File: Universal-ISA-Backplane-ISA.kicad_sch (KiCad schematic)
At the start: 1 part, among them J301 Bus_ISA_16bit

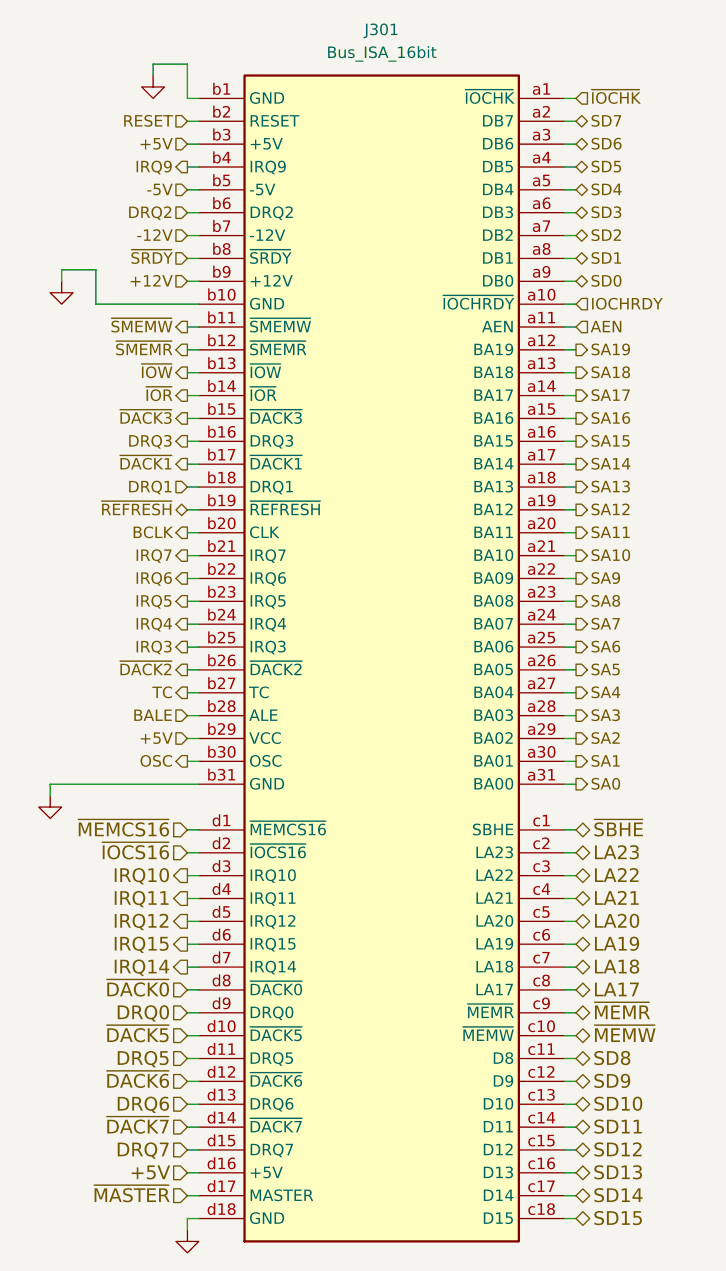
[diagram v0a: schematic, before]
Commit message: PC/104 and ISA connector fixes
And further development
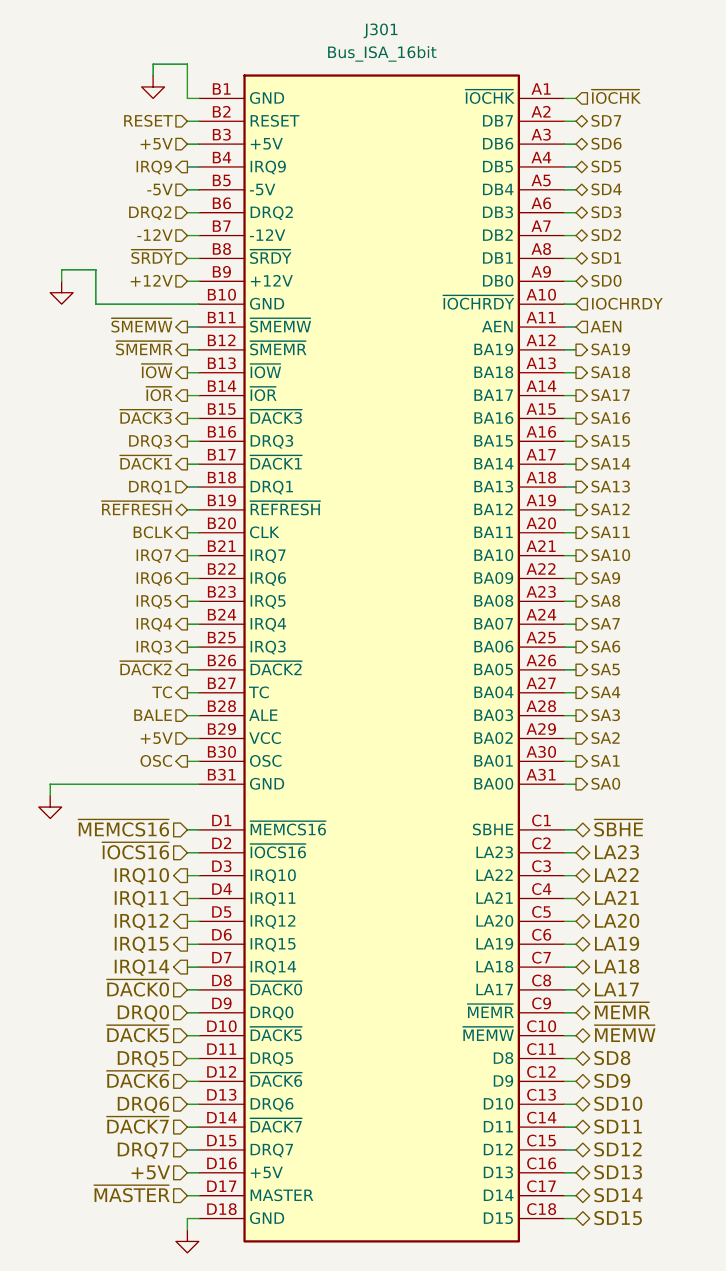
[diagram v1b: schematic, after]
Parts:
- J301: symbol Connector1:Bus_ISA_16bit -> Universal-ISA-Backplane-symbols:Bus_ISA_16bit
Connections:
- net +12V: now also J301.B9 (+12V); no longer J301.b9 (+12V)
- net +5V: now also J301.B29 (VCC), J301.B3 (+5V), J301.D16 (+5V); no longer J301.b29 (VCC), J301.b3 (+5V), J301.d16 (+5V)
- net -12V: now also J301.B7 (-12V); no longer J301.b7 (-12V)
- net -5V: now also J301.B5 (-5V); no longer J301.b5 (-5V)
- net AEN: now also J301.A11 (AEN); no longer J301.a11 (AEN)
- net BALE: now also J301.B28 (ALE); no longer J301.b28 (ALE)
- net BCLK: now also J301.B20 (CLK); no longer J301.b20 (CLK)
- net DRQ0: now also J301.D9 (DRQ0); no longer J301.d9 (DRQ0)
- net DRQ1: now also J301.B18 (DRQ1); no longer J301.b18 (DRQ1)
- net DRQ2: now also J301.B6 (DRQ2); no longer J301.b6 (DRQ2)
- net DRQ3: now also J301.B16 (DRQ3); no longer J301.b16 (DRQ3)
- net DRQ5: now also J301.D11 (DRQ5); no longer J301.d11 (DRQ5)
- net DRQ6: now also J301.D13 (DRQ6); no longer J301.d13 (DRQ6)
- net DRQ7: now also J301.D15 (DRQ7); no longer J301.d15 (DRQ7)
- net GND: now also J301.B1 (GND), J301.B10 (GND), J301.B31 (GND), J301.D18 (GND); no longer J301.b1 (GND), J301.b10 (GND), J301.b31 (GND), J301.d18 (GND)
- net IOCHRDY: now also J301.A10 (~{IOCHRDY}); no longer J301.a10 (~{IOCHRDY})
- net IRQ10: now also J301.D3 (IRQ10); no longer J301.d3 (IRQ10)
- net IRQ11: now also J301.D4 (IRQ11); no longer J301.d4 (IRQ11)
- net IRQ12: now also J301.D5 (IRQ12); no longer J301.d5 (IRQ12)
- net IRQ14: now also J301.D7 (IRQ14); no longer J301.d7 (IRQ14)
- net IRQ15: now also J301.D6 (IRQ15); no longer J301.d6 (IRQ15)
- net IRQ3: now also J301.B25 (IRQ3); no longer J301.b25 (IRQ3)
- net IRQ4: now also J301.B24 (IRQ4); no longer J301.b24 (IRQ4)
- net IRQ5: now also J301.B23 (IRQ5); no longer J301.b23 (IRQ5)
- net IRQ6: now also J301.B22 (IRQ6); no longer J301.b22 (IRQ6)
- net IRQ7: now also J301.B21 (IRQ7); no longer J301.b21 (IRQ7)
- net IRQ9: now also J301.B4 (IRQ9); no longer J301.b4 (IRQ9)
- net LA17: now also J301.C8 (LA17); no longer J301.c8 (LA17)
- net LA18: now also J301.C7 (LA18); no longer J301.c7 (LA18)
- net LA19: now also J301.C6 (LA19); no longer J301.c6 (LA19)
- net LA20: now also J301.C5 (LA20); no longer J301.c5 (LA20)
- net LA21: now also J301.C4 (LA21); no longer J301.c4 (LA21)
- net LA22: now also J301.C3 (LA22); no longer J301.c3 (LA22)
- net LA23: now also J301.C2 (LA23); no longer J301.c2 (LA23)
- net OSC: now also J301.B30 (OSC); no longer J301.b30 (OSC)
- net RESET: now also J301.B2 (RESET); no longer J301.b2 (RESET)
- net SA0: now also J301.A31 (BA00); no longer J301.a31 (BA00)
- net SA1: now also J301.A30 (BA01); no longer J301.a30 (BA01)
- net SA10: now also J301.A21 (BA10); no longer J301.a21 (BA10)
- net SA11: now also J301.A20 (BA11); no longer J301.a20 (BA11)
- net SA12: now also J301.A19 (BA12); no longer J301.a19 (BA12)
- net SA13: now also J301.A18 (BA13); no longer J301.a18 (BA13)
- net SA14: now also J301.A17 (BA14); no longer J301.a17 (BA14)
- net SA15: now also J301.A16 (BA15); no longer J301.a16 (BA15)
- net SA16: now also J301.A15 (BA16); no longer J301.a15 (BA16)
- net SA17: now also J301.A14 (BA17); no longer J301.a14 (BA17)
- net SA18: now also J301.A13 (BA18); no longer J301.a13 (BA18)
- net SA19: now also J301.A12 (BA19); no longer J301.a12 (BA19)
- net SA2: now also J301.A29 (BA02); no longer J301.a29 (BA02)
- net SA3: now also J301.A28 (BA03); no longer J301.a28 (BA03)
- net SA4: now also J301.A27 (BA04); no longer J301.a27 (BA04)
- net SA5: now also J301.A26 (BA05); no longer J301.a26 (BA05)
- net SA6: now also J301.A25 (BA06); no longer J301.a25 (BA06)
- net SA7: now also J301.A24 (BA07); no longer J301.a24 (BA07)
- net SA8: now also J301.A23 (BA08); no longer J301.a23 (BA08)
- net SA9: now also J301.A22 (BA09); no longer J301.a22 (BA09)
- net SD0: now also J301.A9 (DB0); no longer J301.a9 (DB0)
- net SD1: now also J301.A8 (DB1); no longer J301.a8 (DB1)
- net SD10: now also J301.C13 (D10); no longer J301.c13 (D10)
- net SD11: now also J301.C14 (D11); no longer J301.c14 (D11)
- net SD12: now also J301.C15 (D12); no longer J301.c15 (D12)
- net SD13: now also J301.C16 (D13); no longer J301.c16 (D13)
- net SD14: now also J301.C17 (D14); no longer J301.c17 (D14)
- net SD15: now also J301.C18 (D15); no longer J301.c18 (D15)
- net SD2: now also J301.A7 (DB2); no longer J301.a7 (DB2)
- net SD3: now also J301.A6 (DB3); no longer J301.a6 (DB3)
- net SD4: now also J301.A5 (DB4); no longer J301.a5 (DB4)
- net SD5: now also J301.A4 (DB5); no longer J301.a4 (DB5)
- net SD6: now also J301.A3 (DB6); no longer J301.a3 (DB6)
- net SD7: now also J301.A2 (DB7); no longer J301.a2 (DB7)
- net SD8: now also J301.C11 (D8); no longer J301.c11 (D8)
- net SD9: now also J301.C12 (D9); no longer J301.c12 (D9)
- net TC: now also J301.B27 (TC); no longer J301.b27 (TC)
- net ~{DACK0}: now also J301.D8 (~{DACK0}); no longer J301.d8 (~{DACK0})
- net ~{DACK1}: now also J301.B17 (~{DACK1}); no longer J301.b17 (~{DACK1})
- net ~{DACK2}: now also J301.B26 (~{DACK2}); no longer J301.b26 (~{DACK2})
- net ~{DACK3}: now also J301.B15 (~{DACK3}); no longer J301.b15 (~{DACK3})
- net ~{DACK5}: now also J301.D10 (~{DACK5}); no longer J301.d10 (~{DACK5})
- net ~{DACK6}: now also J301.D12 (~{DACK6}); no longer J301.d12 (~{DACK6})
- net ~{DACK7}: now also J301.D14 (~{DACK7}); no longer J301.d14 (~{DACK7})
- net ~{IOCHK}: now also J301.A1 (~{IOCHK}); no longer J301.a1 (~{IOCHK})
- net ~{IOCS16}: now also J301.D2 (~{IOCS16}); no longer J301.d2 (~{IOCS16})
- net ~{IOR}: now also J301.B14 (~{IOR}); no longer J301.b14 (~{IOR})
- net ~{IOW}: now also J301.B13 (~{IOW}); no longer J301.b13 (~{IOW})
- net ~{MASTER}: now also J301.D17 (MASTER); no longer J301.d17 (MASTER)
- net ~{MEMCS16}: now also J301.D1 (~{MEMCS16}); no longer J301.d1 (~{MEMCS16})
- net ~{MEMR}: now also J301.C9 (~{MEMR}); no longer J301.c9 (~{MEMR})
- net ~{MEMW}: now also J301.C10 (~{MEMW}); no longer J301.c10 (~{MEMW})
- net ~{REFRESH}: now also J301.B19 (~{REFRESH}); no longer J301.b19 (~{REFRESH})
- net ~{SBHE}: now also J301.C1 (SBHE); no longer J301.c1 (SBHE)
- net ~{SMEMR}: now also J301.B12 (~{SMEMR}); no longer J301.b12 (~{SMEMR})
- net ~{SMEMW}: now also J301.B11 (~{SMEMW}); no longer J301.b11 (~{SMEMW})
- net ~{SRDY}: now also J301.B8 (~{SRDY}); no longer J301.b8 (~{SRDY})
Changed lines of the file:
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@@
+    (stroke (width 0) (type default) (color 0 0 0 0))
+  )
+  (wire (pts (xy 120.65 160.02) (xy 120.65 161.29))
     (stroke (width 0) (type default) (color 0 0 0 0))
   )
@@
   )
   (wire (pts (xy 121.92 154.94) (xy 120.65 154.94))
-    (stroke (width 0) (type default) (color 0 0 0 0))
-  )
-  (wire (pts (xy 120.65 161.29) (xy 120.65 160.02))
     (stroke (width 0) (type default) (color 0 0 0 0))
   )
@@
     (pin "1")
   )
-  (symbol (lib_id "Connector1:Bus_ISA_16bit") (at 142.24 99.06 0) (unit 1)
+  (symbol (lib_id "Universal-ISA-Backplane-symbols:Bus_ISA_16bit") (at 142.24 99.06 0) (unit 1)
     (in_bom yes) (on_board yes) (fields_autoplaced)
     (property "Reference" "J301" (id 0) (at 142.24 27.94 0))
@@
       (effects (font (size 1.27 1.27)) hide)
     )
-    (property "Datasheet" "https://en.wikipedia.org/wiki/Industry_Standard_Architecture" (id 3) (at 142.24 97.79 0)
-      (effects (font (size 1.27 1.27)) hide)
-    )
-    (pin "a1")
-    (pin "a10")
-    (pin "a11")
-    (pin "a12")
-    (pin "a13")
-    (pin "a14")
-    (pin "a15")
-    (pin "a16")
-    (pin "a17")
-    (pin "a18")
-    (pin "a19")
-    (pin "a2")
-    (pin "a20")
-    (pin "a21")
-    (pin "a22")
-    (pin "a23")
-    (pin "a24")
-    (pin "a25")
-    (pin "a26")
-    (pin "a27")
-    (pin "a28")
-    (pin "a29")
-    (pin "a3")
-    (pin "a30")
-    (pin "a31")
-    (pin "a4")
-    (pin "a5")
-    (pin "a6")
-    (pin "a7")
-    (pin "a8")
-    (pin "a9")
-    (pin "b1")
-    (pin "b10")
-    (pin "b11")
-    (pin "b12")
-    (pin "b13")
-    (pin "b14")
-    (pin "b15")
-    (pin "b16")
-    (pin "b17")
-    (pin "b18")
-    (pin "b19")
-    (pin "b2")
-    (pin "b20")
-    (pin "b21")
-    (pin "b22")
-    (pin "b23")
-    (pin "b24")
-    (pin "b25")
-    (pin "b26")
-    (pin "b27")
-    (pin "b28")
-    (pin "b29")
-    (pin "b3")
-    (pin "b30")
-    (pin "b31")
-    (pin "b4")
-    (pin "b5")
-    (pin "b6")
-    (pin "b7")
-    (pin "b8")
-    (pin "b9")
-    (pin "c1")
-    (pin "c10")
-    (pin "c11")
-    (pin "c12")
-    (pin "c13")
-    (pin "c14")
-    (pin "c15")
-    (pin "c16")
-    (pin "c17")
-    (pin "c18")
-    (pin "c2")
-    (pin "c3")
-    (pin "c4")
-    (pin "c5")
-    (pin "c6")
-    (pin "c7")
-    (pin "c8")
-    (pin "c9")
-    (pin "d1")
-    (pin "d10")
-    (pin "d11")
-    (pin "d12")
-    (pin "d13")
-    (pin "d14")
-    (pin "d15")
-    (pin "d16")
-    (pin "d17")
-    (pin "d18")
-    (pin "d2")
-    (pin "d3")
-    (pin "d4")
-    (pin "d5")
-    (pin "d6")
-    (pin "d7")
-    (pin "d8")
-    (pin "d9")
+    (property "Datasheet" "https://en.wikipedia.org/wiki/Industry_Standard_Architecture" (id 3) (at 142.24 170.18 0)
+      (effects (font (size 1.27 1.27)) hide)
+    )
+    (pin "A1")
+    (pin "A10")
+    (pin "A11")
+    (pin "A12")
+    (pin "A13")
+    (pin "A14")
+    (pin "A15")
+    (pin "A16")
+    (pin "A17")
+    (pin "A18")
+    (pin "A19")
+    (pin "A2")
+    (pin "A20")
+    (pin "A21")
+    (pin "A22")
+    (pin "A23")
+    (pin "A24")
+    (pin "A25")
+    (pin "A26")
+    (pin "A27")
+    (pin "A28")
+    (pin "A29")
+    (pin "A3")
+    (pin "A30")
+    (pin "A31")
+    (pin "A4")
+    (pin "A5")
+    (pin "A6")
+    (pin "A7")
+    (pin "A8")
+    (pin "A9")
+    (pin "B1")
+    (pin "B10")
+    (pin "B11")
+    (pin "B12")
+    (pin "B13")
+    (pin "B14")
+    (pin "B15")
+    (pin "B16")
+    (pin "B17")
+    (pin "B18")
+    (pin "B19")
+    (pin "B2")
+    (pin "B20")
+    (pin "B21")
+    (pin "B22")
+    (pin "B23")
+    (pin "B24")
+    (pin "B25")
+    (pin "B26")
+    (pin "B27")
+    (pin "B28")
+    (pin "B29")
+    (pin "B3")
+    (pin "B30")
+    (pin "B31")
+    (pin "B4")
+    (pin "B5")
+    (pin "B6")
+    (pin "B7")
+    (pin "B8")
+    (pin "B9")
+    (pin "C1")
+    (pin "C10")
+    (pin "C11")
+    (pin "C12")
+    (pin "C13")
+    (pin "C14")
+    (pin "C15")
+    (pin "C16")
+    (pin "C17")
+    (pin "C18")
+    (pin "C2")
+    (pin "C3")
+    (pin "C4")
+    (pin "C5")
+    (pin "C6")
+    (pin "C7")
+    (pin "C8")
+    (pin "C9")
+    (pin "D1")
+    (pin "D10")
+    (pin "D11")
+    (pin "D12")
+    (pin "D13")
+    (pin "D14")
+    (pin "D15")
+    (pin "D16")
+    (pin "D17")
+    (pin "D18")
+    (pin "D2")
+    (pin "D3")
+    (pin "D4")
+    (pin "D5")
+    (pin "D6")
+    (pin "D7")
+    (pin "D8")
+    (pin "D9")
   )
 )

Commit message: Kicad resave fixup
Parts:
- J301: footprint (none) -> Universal-ISA-Backplane:ISA16
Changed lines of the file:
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@@
     (property "Reference" "J301" (id 0) (at 142.24 27.94 0))
     (property "Value" "Bus_ISA_16bit" (id 1) (at 142.24 30.48 0))
-    (property "Footprint" "" (id 2) (at 142.24 97.79 0)
+    (property "Footprint" "Universal-ISA-Backplane:ISA16" (id 2) (at 142.24 97.79 0)
       (effects (font (size 1.27 1.27)) hide)
     )
